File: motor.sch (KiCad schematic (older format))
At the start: 43 parts, among them J5 70543-0003, Q35 IRLML0030TRPbF, Q36 IRLML0030TRPbF, Q37 IRLML0030TRPbF, Q38 IRLML0030TRPbF, Q39 IRLML0030TRPbF, Q40 IRLML0030TRPbF, Q41 IRLML0030TRPbF, Q42 IRLML0030TRPbF, U6 TMC2160-TA

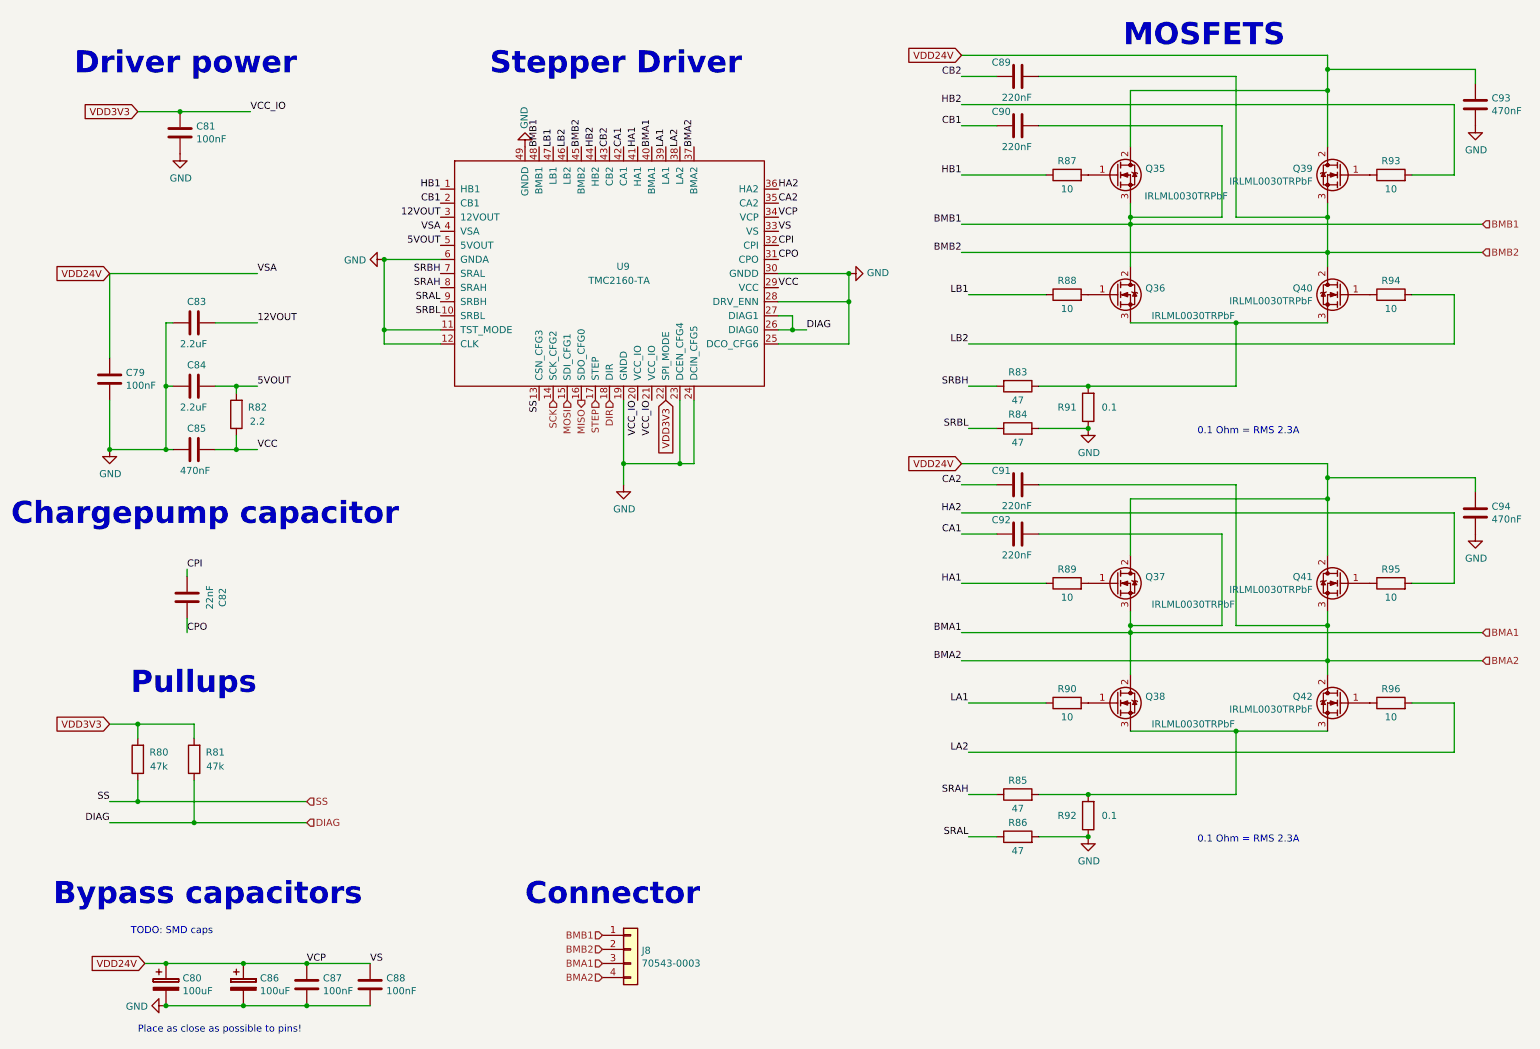
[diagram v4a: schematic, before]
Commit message: Add PU for SD_DETECT_PIN
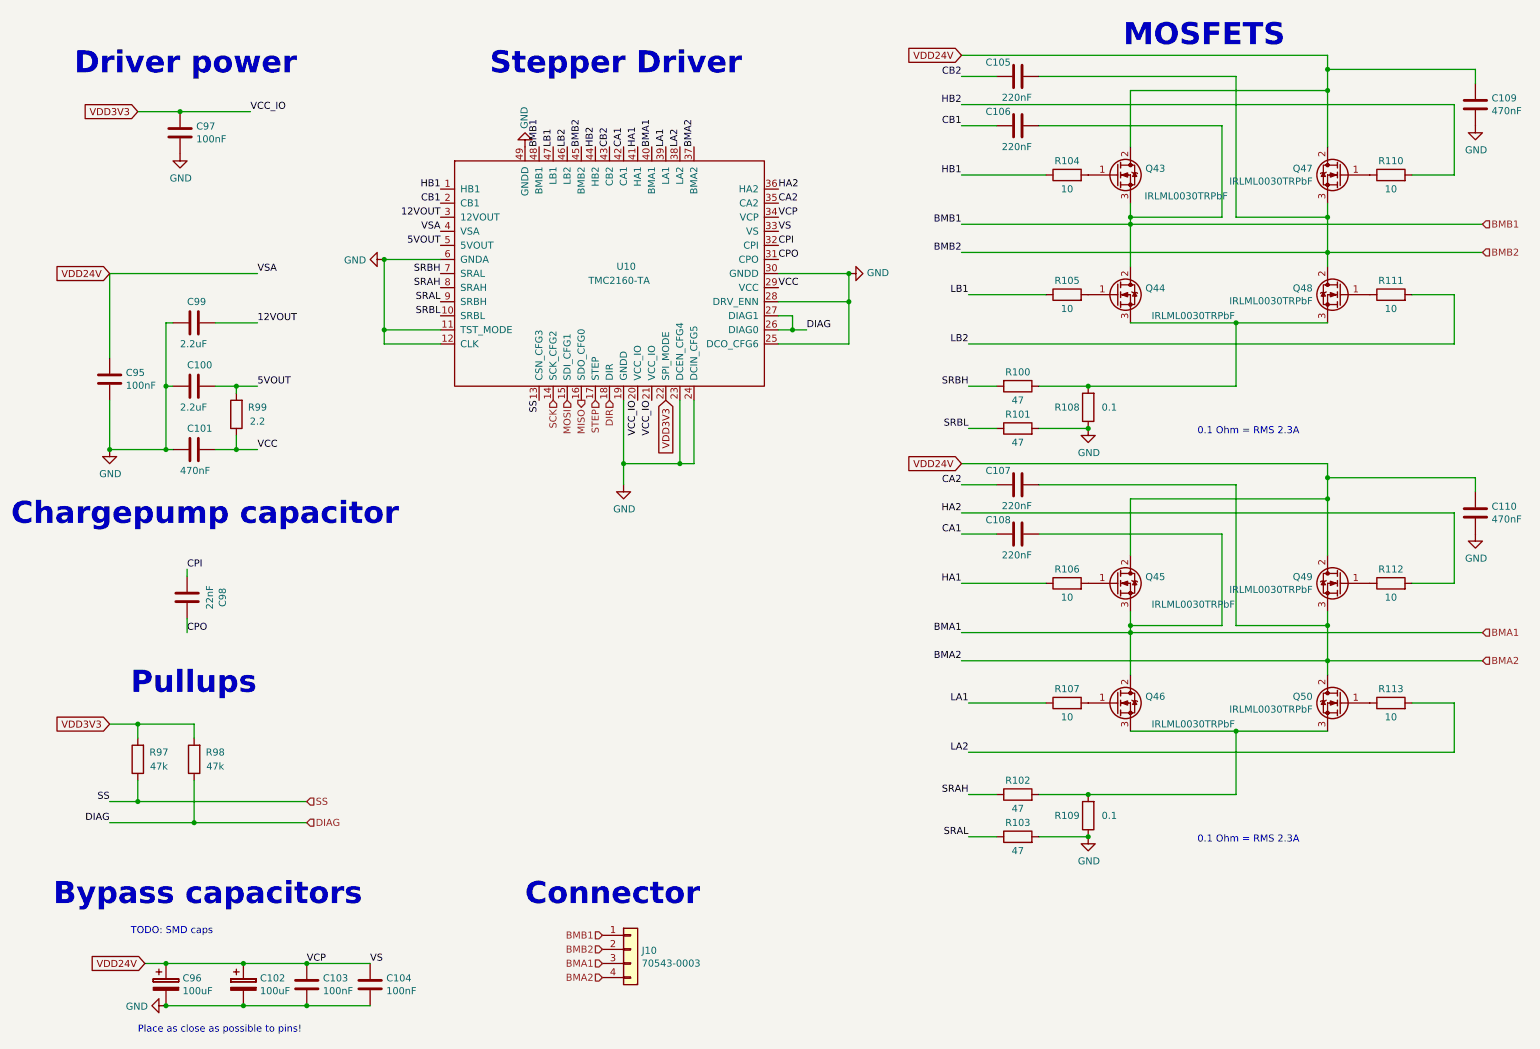
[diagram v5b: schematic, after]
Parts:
- renumbered J5 to J6

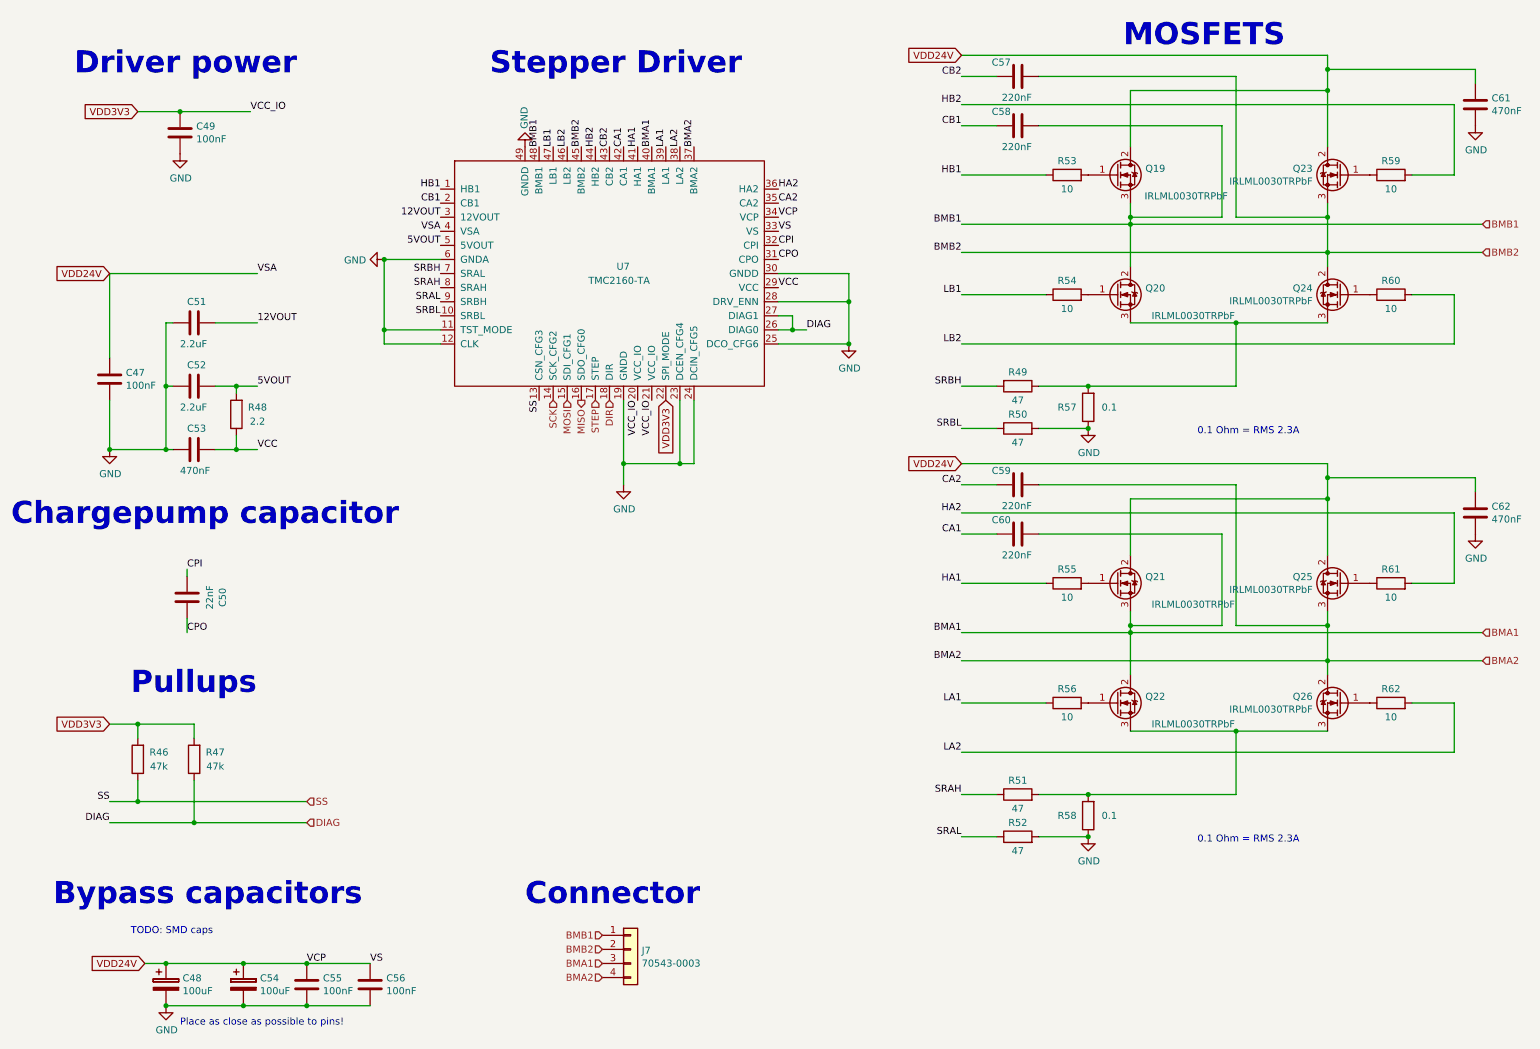
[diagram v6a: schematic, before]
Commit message: Further Improved Readability - Rotated labels
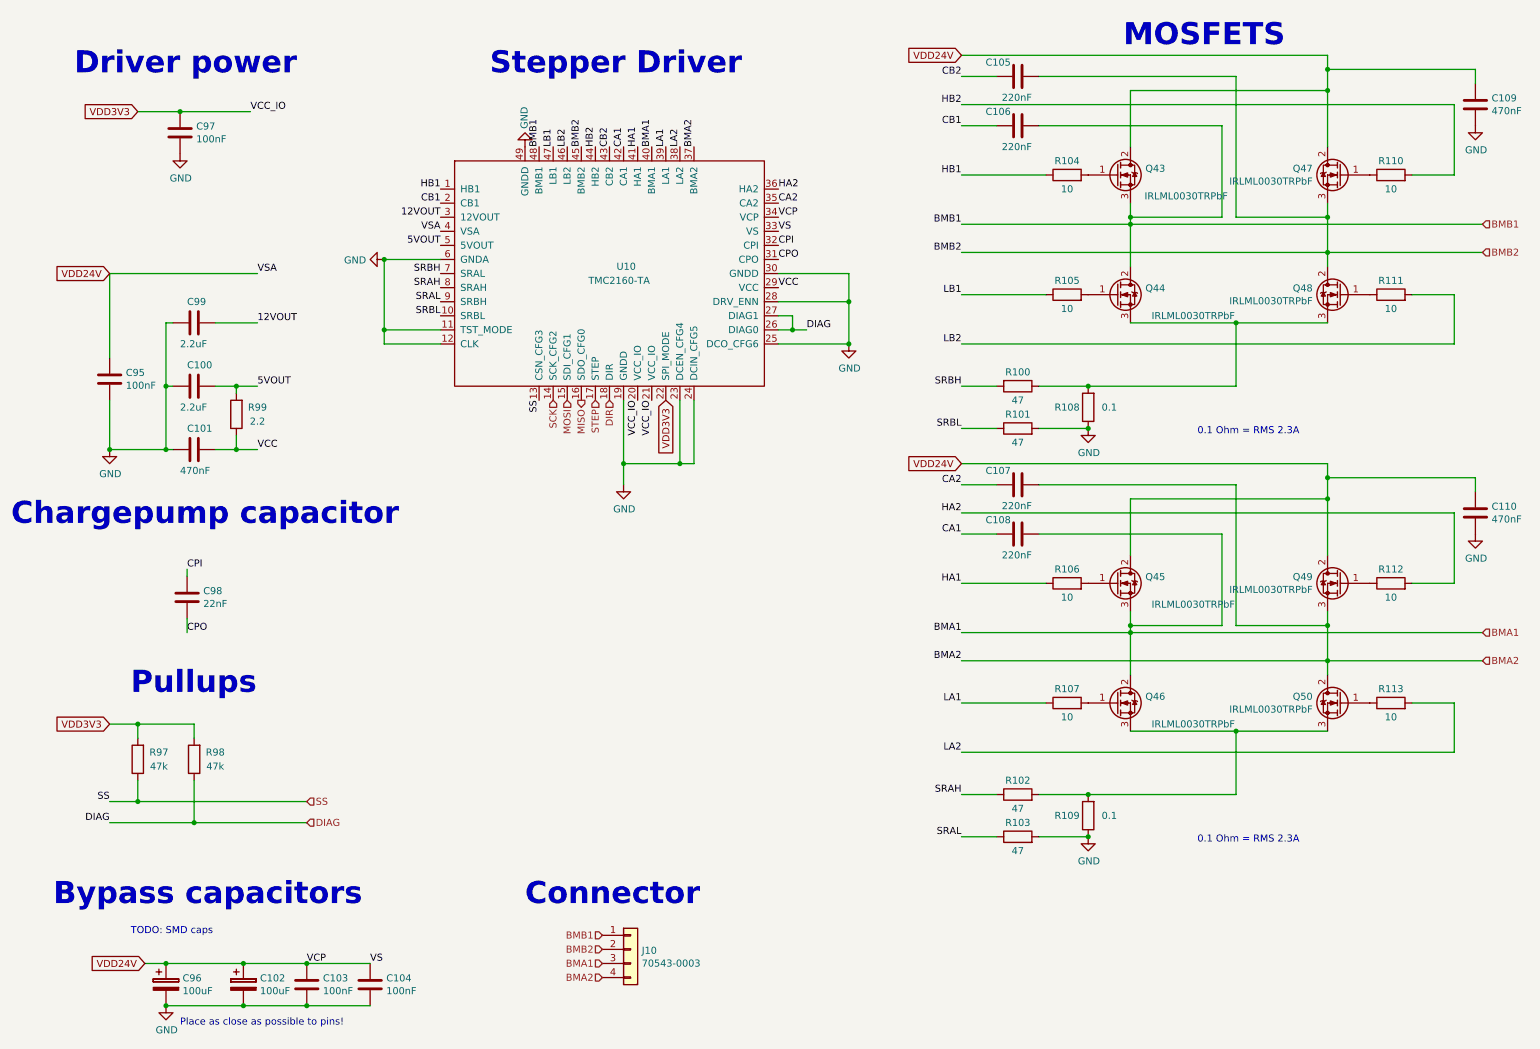
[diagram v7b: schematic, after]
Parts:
- removed C34: 22nF, Capacitor_SMD:C_0603_1608Metric, symbol Device:C
- added C98: 22nF, Capacitor_SMD:C_0603_1608Metric, symbol Device:C
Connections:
- net CPI: now also C98.1
- net CPO: now also C98.2

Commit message: Re-place some items that had broken timestamps
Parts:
- renumbered C98 to C34
